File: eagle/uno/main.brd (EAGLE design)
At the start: 37.8 x 40.6 mm, 10 parts

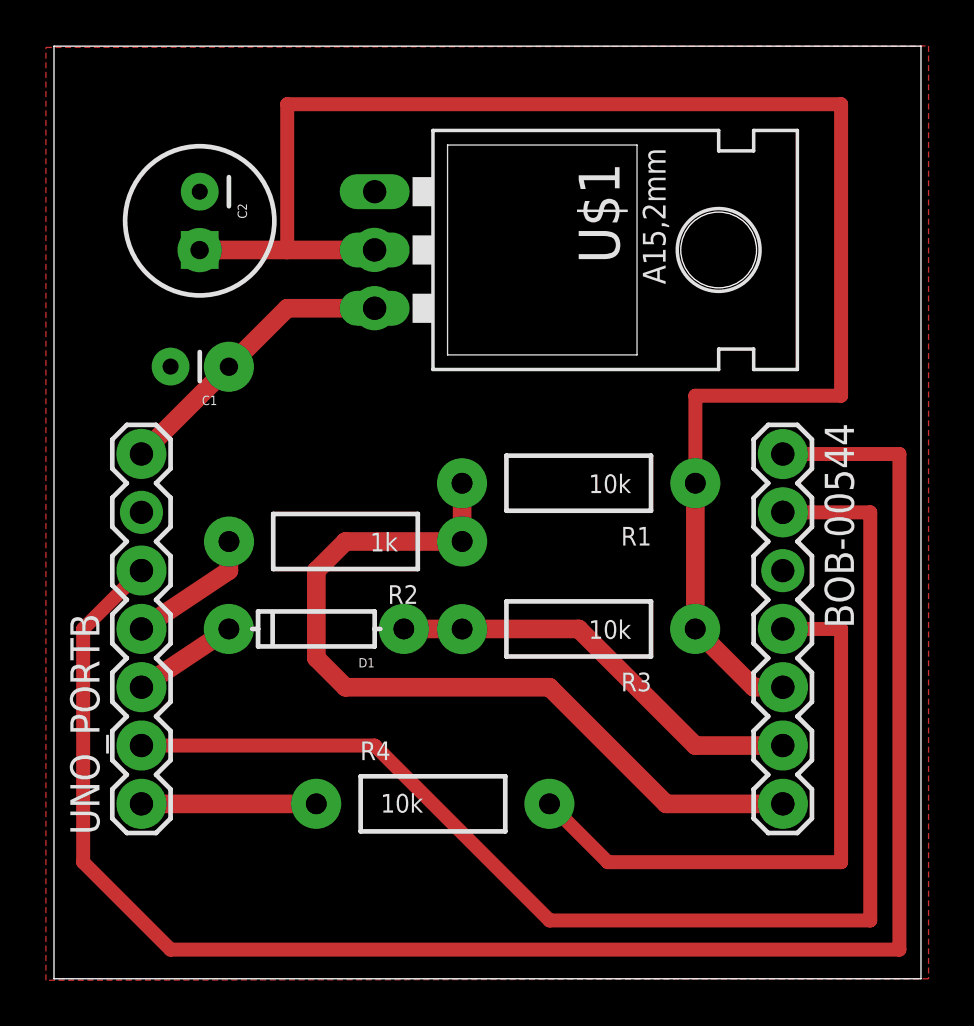
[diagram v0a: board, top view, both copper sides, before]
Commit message: [ update ] eagle/uno, rotate sdcard board connector
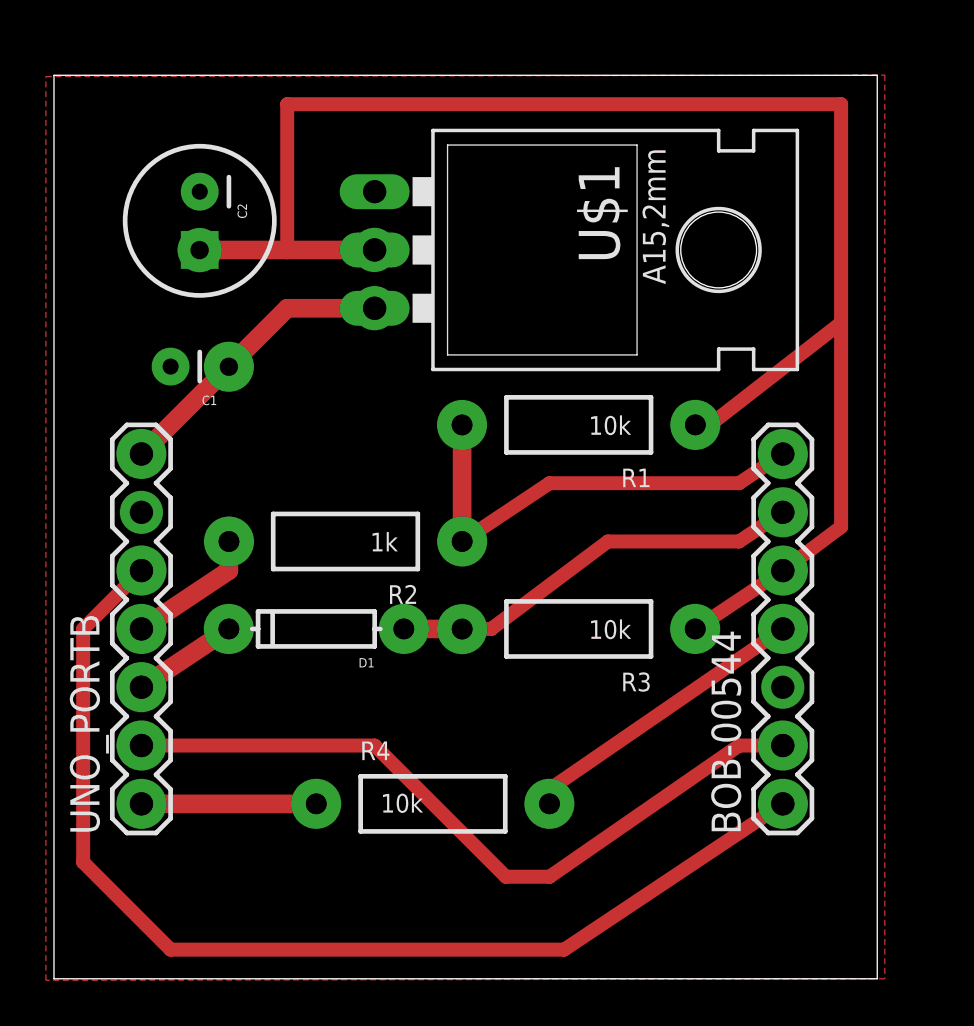
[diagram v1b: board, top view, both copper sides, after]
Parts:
- moved BOB-00544 15.2 mm to (30.5, 2.54), turned to 90 degrees
- moved R1 2.54 mm to (21.6, 19.1)
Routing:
- net CD: track 77.6 -> 47.7 mm
- net SPI_MISO: track 56.5 -> 32.1 mm
- net CS: track 36.2 -> 20.2 mm
- net SCK: track 26.5 -> 13.0 mm
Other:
- board size 37.8 x 40.6 mm -> 35.9 x 39.4 mm
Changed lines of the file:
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@@
 <setting verticaltext="up"/>
 </settings>
-<grid distance="0.025" unitdist="inch" unit="inch" style="lines" multiple="1" display="yes" altdistance="0.025" altunitdist="inch" altunit="inch"/>
+<grid distance="0.635" unitdist="mm" unit="mm" style="lines" multiple="1" display="yes" altdistance="0.025" altunitdist="inch" altunit="inch"/>
 <layers>
 <layer number="1" name="Top" color="4" fill="1" visible="yes" active="yes"/>
@@
 <board>
 <plain>
-<wire x1="-1.27" y1="-5.08" x2="36.5" y2="-5.08" width="0" layer="20"/>
-<wire x1="36.5" y1="-5.08" x2="36.5" y2="35.55" width="0" layer="20"/>
-<wire x1="36.5" y1="35.55" x2="-1.27" y2="35.55" width="0" layer="20"/>
-<wire x1="-1.27" y1="35.55" x2="-1.27" y2="-5.08" width="0" layer="20"/>
+<wire x1="-1.27" y1="-5.08" x2="34.595" y2="-5.08" width="0" layer="20"/>
+<wire x1="34.595" y1="-5.08" x2="34.595" y2="34.28" width="0" layer="20"/>
+<wire x1="34.595" y1="34.28" x2="-1.27" y2="34.28" width="0" layer="20"/>
+<wire x1="-1.27" y1="34.28" x2="-1.27" y2="-5.08" width="0" layer="20"/>
 </plain>
 <attributes>
@@
 </autorouter>
 <elements>
-<element name="BOB-00544" library="SparkFun" package="1X07" value="" x="30.48" y="17.78" rot="R270"/>
+<element name="BOB-00544" library="SparkFun" package="1X07" value="" x="30.48" y="2.54" rot="R90"/>
 <element name="UNO_PORTB" library="SparkFun" package="1X07" value="" x="2.54" y="2.54" rot="R90"/>
-<element name="R1" library="SparkFun" package="AXIAL-0.4" value="10k" x="21.59" y="16.51" rot="R180"/>
+<element name="R1" library="SparkFun" package="AXIAL-0.4" value="10k" x="21.59" y="19.05" rot="R180"/>
 <element name="R2" library="SparkFun" package="AXIAL-0.4" value="1k" x="11.43" y="13.97" rot="R180"/>
 <element name="R3" library="SparkFun" package="AXIAL-0.4" value="10k" x="21.59" y="10.16" rot="R180"/>
@@
 <contactref element="R1" pad="P$2"/>
 <contactref element="R2" pad="P$1"/>
-<wire x1="16.51" y1="16.51" x2="16.51" y2="13.97" width="0.8128" layer="1"/>
-<wire x1="10.16" y1="8.89" x2="11.43" y2="7.62" width="0.8128" layer="1"/>
-<wire x1="11.43" y1="7.62" x2="20.32" y2="7.62" width="0.8128" layer="1"/>
-<wire x1="20.32" y1="7.62" x2="25.4" y2="2.54" width="0.8128" layer="1"/>
-<wire x1="25.4" y1="2.54" x2="30.48" y2="2.54" width="0.8128" layer="1"/>
-<wire x1="10.16" y1="8.89" x2="10.16" y2="12.7" width="0.8128" layer="1"/>
-<wire x1="10.16" y1="12.7" x2="11.43" y2="13.97" width="0.8128" layer="1"/>
-<wire x1="11.43" y1="13.97" x2="16.51" y2="13.97" width="0.8128" layer="1"/>
+<wire x1="16.51" y1="19.05" x2="16.51" y2="13.97" width="0.8128" layer="1"/>
+<wire x1="30.48" y1="17.78" x2="28.575" y2="16.51" width="0.6096" layer="1"/>
+<wire x1="28.575" y1="16.51" x2="20.32" y2="16.51" width="0.6096" layer="1"/>
+<wire x1="20.32" y1="16.51" x2="16.51" y2="13.97" width="0.6096" layer="1"/>
 </signal>
 <signal name="DI">
@@
 <contactref element="D1" pad="A"/>
 <wire x1="13.97" y1="10.16" x2="16.51" y2="10.16" width="0.8128" layer="1"/>
-<wire x1="30.48" y1="5.08" x2="26.67" y2="5.08" width="0.8128" layer="1"/>
-<wire x1="26.67" y1="5.08" x2="21.59" y2="10.16" width="0.8128" layer="1"/>
-<wire x1="21.59" y1="10.16" x2="16.51" y2="10.16" width="0.8128" layer="1"/>
+<wire x1="30.48" y1="15.24" x2="28.575" y2="13.97" width="0.6096" layer="1"/>
+<wire x1="28.575" y1="13.97" x2="22.86" y2="13.97" width="0.6096" layer="1"/>
+<wire x1="22.86" y1="13.97" x2="17.78" y2="10.16" width="0.6096" layer="1"/>
+<wire x1="17.78" y1="10.16" x2="16.51" y2="10.16" width="0.6096" layer="1"/>
 </signal>
 <signal name="SCK">
 <contactref element="BOB-00544" pad="4"/>
 <contactref element="R4" pad="P$2"/>
-<wire x1="20.32" y1="2.54" x2="22.86" y2="0" width="0.6096" layer="1"/>
-<wire x1="22.86" y1="0" x2="33.02" y2="0" width="0.6096" layer="1"/>
-<wire x1="33.02" y1="0" x2="33.02" y2="10.16" width="0.6096" layer="1"/>
-<wire x1="33.02" y1="10.16" x2="30.48" y2="10.16" width="0.6096" layer="1"/>
+<wire x1="30.48" y1="10.16" x2="20.32" y2="3.175" width="0.6096" layer="1"/>
+<wire x1="20.32" y1="3.175" x2="20.32" y2="2.54" width="0.6096" layer="1"/>
 </signal>
 <signal name="GND">
@@
 <contactref element="UNO_PORTB" pad="6"/>
 <polygon width="0.3048" layer="1" isolate="0.4064">
-<vertex x="-1.622171875" y="35.49394375"/>
-<vertex x="36.83" y="35.56"/>
-<vertex x="36.83" y="-5.08"/>
+<vertex x="-1.622171875" y="34.22394375"/>
+<vertex x="34.925" y="34.29"/>
+<vertex x="34.925" y="-5.08"/>
 <vertex x="-1.622171875" y="-5.14605625"/>
 </polygon>
@@
 <wire x1="0" y1="10.16" x2="0" y2="0" width="0.6096" layer="1"/>
 <wire x1="0" y1="0" x2="3.81" y2="-3.81" width="0.6096" layer="1"/>
-<wire x1="3.81" y1="-3.81" x2="35.56" y2="-3.81" width="0.6096" layer="1"/>
-<wire x1="35.56" y1="-3.81" x2="35.56" y2="17.78" width="0.6096" layer="1"/>
-<wire x1="35.56" y1="17.78" x2="30.48" y2="17.78" width="0.6096" layer="1"/>
+<wire x1="3.81" y1="-3.81" x2="20.955" y2="-3.81" width="0.6096" layer="1"/>
+<wire x1="20.955" y1="-3.81" x2="30.48" y2="2.54" width="0.6096" layer="1"/>
 </signal>
 <signal name="SPI_SS">
@@
 <contactref element="UNO_PORTB" pad="2"/>
 <wire x1="2.54" y1="5.08" x2="12.7" y2="5.08" width="0.6096" layer="1"/>
-<wire x1="12.7" y1="5.08" x2="20.32" y2="-2.54" width="0.6096" layer="1"/>
-<wire x1="20.32" y1="-2.54" x2="34.29" y2="-2.54" width="0.6096" layer="1"/>
-<wire x1="34.29" y1="-2.54" x2="34.29" y2="15.24" width="0.6096" layer="1"/>
-<wire x1="34.29" y1="15.24" x2="30.48" y2="15.24" width="0.6096" layer="1"/>
+<wire x1="12.7" y1="5.08" x2="18.415" y2="-0.635" width="0.6096" layer="1"/>
+<wire x1="18.415" y1="-0.635" x2="20.32" y2="-0.635" width="0.6096" layer="1"/>
+<wire x1="20.32" y1="-0.635" x2="28.575" y2="5.08" width="0.6096" layer="1"/>
+<wire x1="28.575" y1="5.08" x2="30.48" y2="5.08" width="0.6096" layer="1"/>
 </signal>
 <signal name="SPI_SCK">
@@
 <contactref element="R3" pad="P$1"/>
 <contactref element="BOB-00544" pad="5"/>
-<wire x1="26.67" y1="16.51" x2="26.67" y2="10.16" width="0.8128" layer="1"/>
-<wire x1="26.67" y1="10.16" x2="29.21" y2="7.62" width="0.8128" layer="1"/>
-<wire x1="29.21" y1="7.62" x2="30.48" y2="7.62" width="0.8128" layer="1"/>
 <wire x1="5.08" y1="26.67" x2="8.89" y2="26.67" width="0.8128" layer="1"/>
 <wire x1="8.89" y1="26.67" x2="12.7" y2="26.67" width="0.8128" layer="1"/>
-<wire x1="26.67" y1="16.51" x2="26.67" y2="20.32" width="0.6096" layer="1"/>
-<wire x1="26.67" y1="20.32" x2="33.02" y2="20.32" width="0.6096" layer="1"/>
-<wire x1="33.02" y1="20.32" x2="33.02" y2="33.02" width="0.6096" layer="1"/>
+<wire x1="26.67" y1="19.05" x2="27.305" y2="19.05" width="0.6096" layer="1"/>
+<wire x1="27.305" y1="19.05" x2="33.02" y2="23.495" width="0.6096" layer="1"/>
+<wire x1="33.02" y1="23.495" x2="33.02" y2="33.02" width="0.6096" layer="1"/>
 <wire x1="33.02" y1="33.02" x2="8.89" y2="33.02" width="0.6096" layer="1"/>
 <wire x1="8.89" y1="33.02" x2="8.89" y2="26.67" width="0.6096" layer="1"/>
+<wire x1="30.48" y1="12.7" x2="33.02" y2="14.605" width="0.6096" layer="1"/>
+<wire x1="33.02" y1="14.605" x2="33.02" y2="23.495" width="0.6096" layer="1"/>
+<wire x1="26.67" y1="10.16" x2="30.48" y2="12.7" width="0.6096" layer="1"/>
 </signal>
 <signal name="N$3">
@@
 </signal>
 <signal name="N$4">
-<via x="16.50618125" y="16.5056375" extent="1-16" drill="0.9" diameter="2.1844"/>
+<via x="16.50618125" y="19.0456375" extent="1-16" drill="0.9" diameter="2.1844"/>
 </signal>
 <signal name="N$5">
@@
 </signal>
 <signal name="N$13">
-<via x="26.66975" y="16.508596875" extent="1-16" drill="0.9" diameter="2.1844"/>
+<via x="26.66975" y="19.048596875" extent="1-16" drill="0.9" diameter="2.1844"/>
 </signal>
 <signal name="N$14">
@@
 </signal>
 <signal name="N$24">
-<via x="30.484959375" y="10.1626875" extent="1-16" drill="1" diameter="2.1844"/>
+<via x="30.484959375" y="12.7026875" extent="1-16" drill="1" diameter="2.1844"/>
 </signal>
 <signal name="N$25">
-<via x="30.487703125" y="7.62228125" extent="1-16" drill="1" diameter="2.1844"/>
+<via x="30.487703125" y="10.16228125" extent="1-16" drill="1" diameter="2.1844"/>
 </signal>
 <signal name="N$26">
